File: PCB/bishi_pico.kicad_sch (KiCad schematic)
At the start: 39 parts, among them SW1 SW_DIP_x01, SW2 SW_DIP_x01, SW3 SW_DIP_x01, SW4 SW_DIP_x01, U1 PiPico_No_SWD, U3 TMAG5273

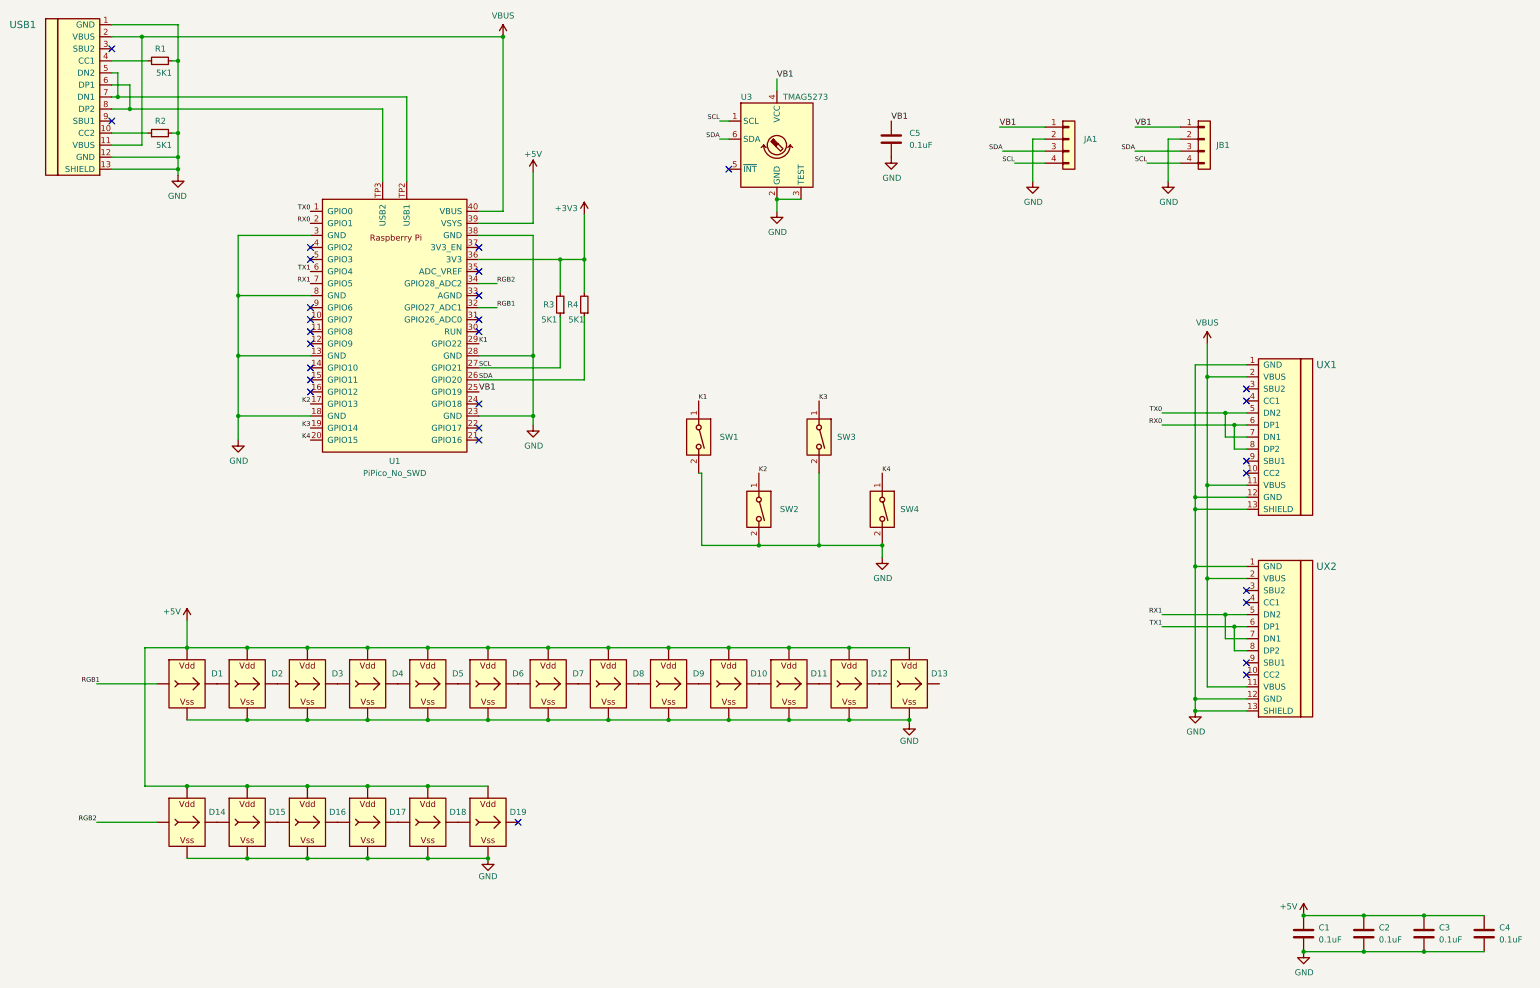
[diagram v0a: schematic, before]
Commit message: PCB v1.1 (ESD diodes added)
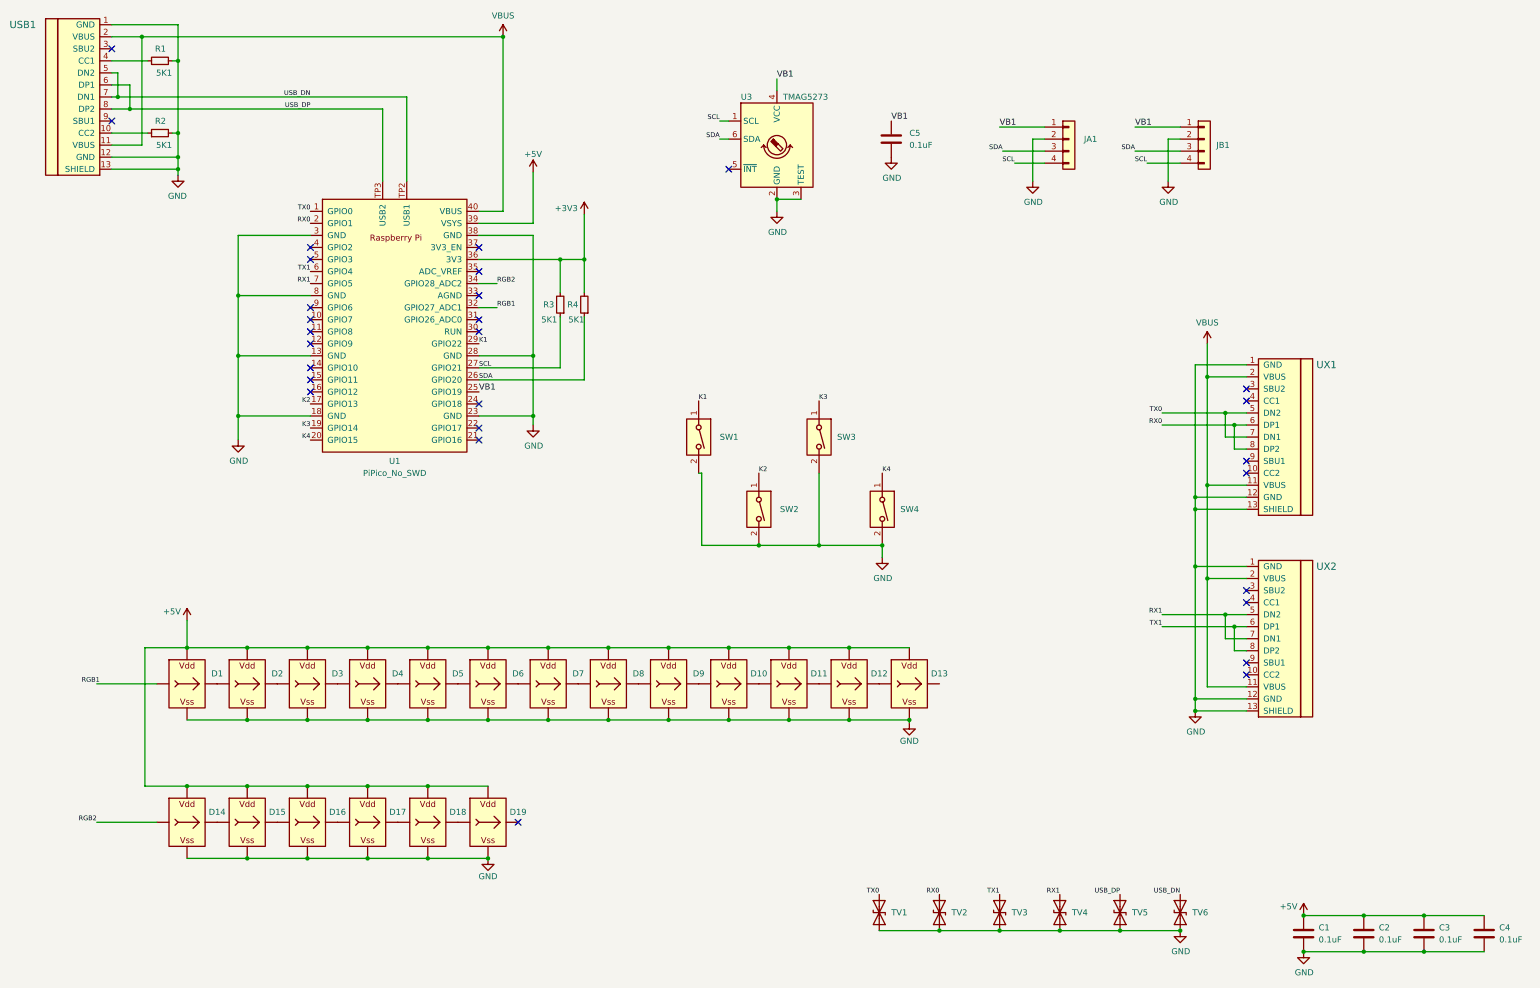
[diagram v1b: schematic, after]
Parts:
- added TV1, TV2, TV3, TV4, TV5, TV6: ESD9B3.3ST5G, Diode_SMD:D_SOD-323_HandSoldering, symbol Diode:ESD9B3.3ST5G
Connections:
- net GND: now also TV1.2 (A2), TV2.2 (A2), TV3.2 (A2), TV4.2 (A2), TV5.2 (A2), TV6.2 (A2)
- net RX0: now also TV2.1 (A1)
- net RX1: now also TV4.1 (A1)
- net TX0: now also TV1.1 (A1)
- net TX1: now also TV3.1 (A1)
- net USB_DN: now reaches U1.TP2 (USB1), USB1.5 (DN2), USB1.7 (DN1)
- net USB_DN: now also TV6.1 (A1)
- net USB_DP: now reaches U1.TP3 (USB2), USB1.6 (DP1), USB1.8 (DP2)
- net USB_DP: now also TV5.1 (A1)
